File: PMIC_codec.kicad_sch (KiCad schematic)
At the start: 18 parts, among them U3 RK809-2

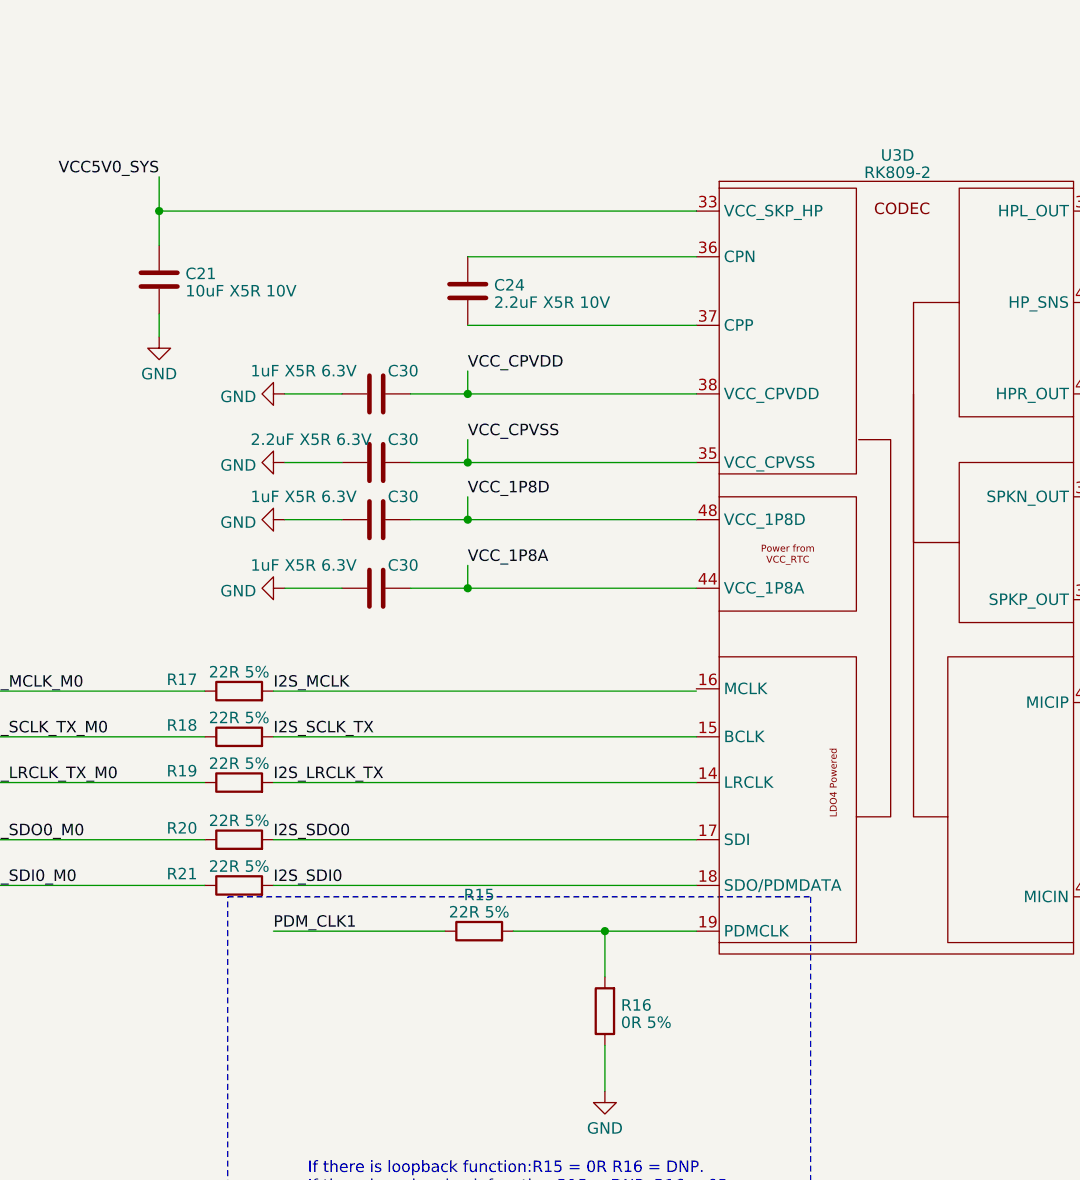
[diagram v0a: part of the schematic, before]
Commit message: updated footprints
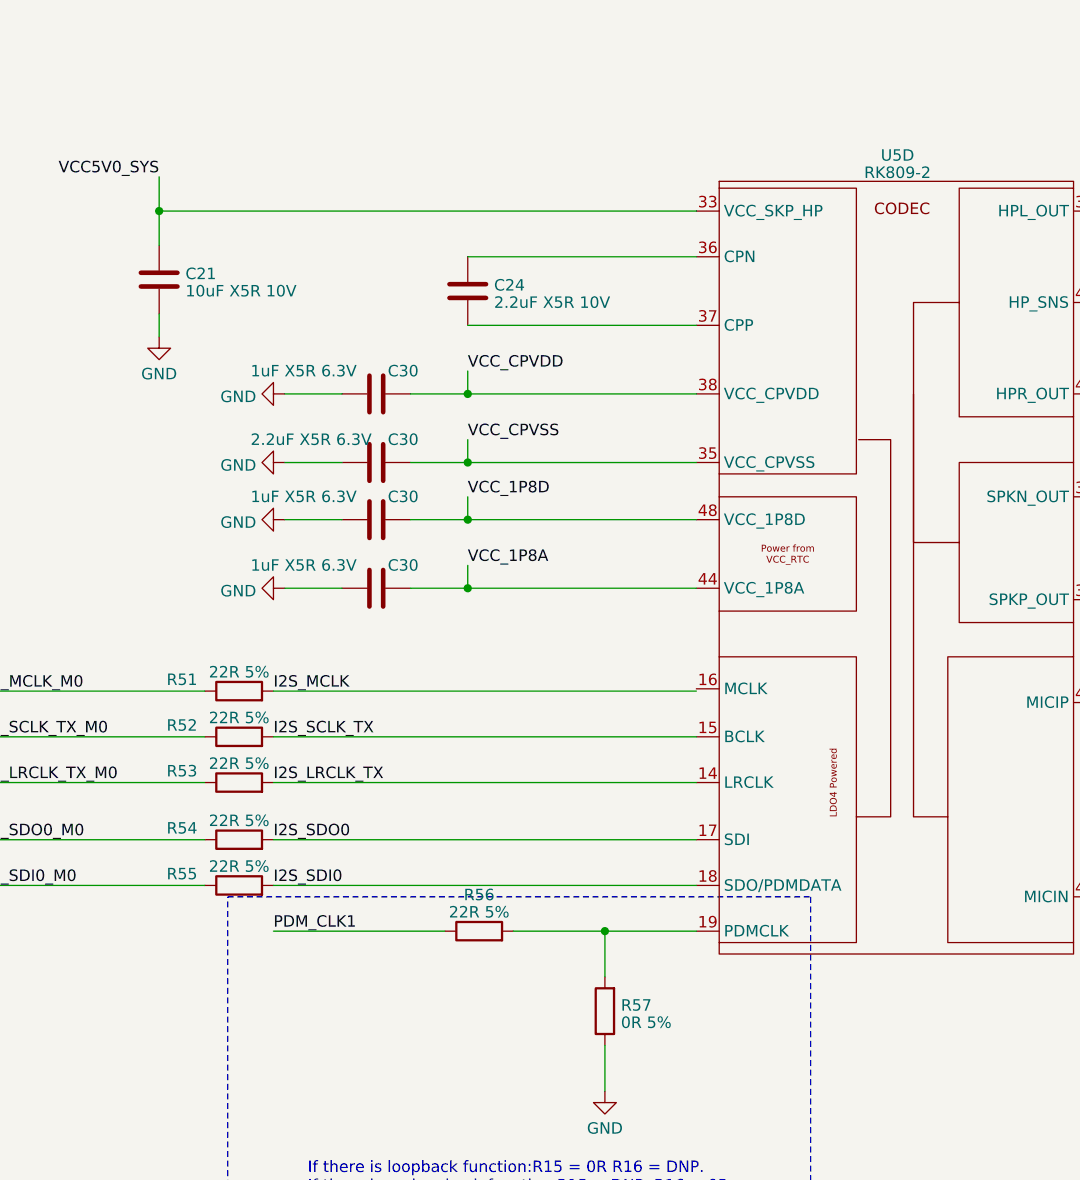
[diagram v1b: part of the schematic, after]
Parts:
- renumbered R17 to R51, R18 to R52, R19 to R53, R20 to R54, R21 to R55, R15 to R56, R16 to R57, U3 to U5
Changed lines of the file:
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@@
         )
         (path "/e3b58043-16a3-43c8-9fad-9c9784eebfa4/cc9fb3ac-19c3-47a8-ba7d-678b4d514ff0/46e9a7bf-8506-4399-90d8-57d007223126/932d3a83-3e3a-47a2-863a-dd551f528f64"
-          (reference "#PWR039") (unit 1)
+          (reference "#PWR0111") (unit 1)
         )
       )
@@
   (symbol (lib_id "CPU_Rockchip:RK809") (at 176.53 67.31 0) (unit 4)
     (in_bom yes) (on_board yes) (dnp no) (fields_autoplaced)
-    (property "Reference" "U3" (at 177.292 35.7251 0)
+    (property "Reference" "U5" (at 177.292 35.7251 0)
       (effects (font (size 1.27 1.27)))
     )
@@
       (project "leaf"
         (path "/e3b58043-16a3-43c8-9fad-9c9784eebfa4/cc9fb3ac-19c3-47a8-ba7d-678b4d514ff0/46e9a7bf-8506-4399-90d8-57d007223126/932d3a83-3e3a-47a2-863a-dd551f528f64"
-          (reference "U3") (unit 4)
+          (reference "U5") (unit 4)
         )
       )
@@
         )
         (path "/e3b58043-16a3-43c8-9fad-9c9784eebfa4/cc9fb3ac-19c3-47a8-ba7d-678b4d514ff0/46e9a7bf-8506-4399-90d8-57d007223126/932d3a83-3e3a-47a2-863a-dd551f528f64"
-          (reference "#PWR038") (unit 1)
+          (reference "#PWR0109") (unit 1)
         )
       )
@@
         )
         (path "/e3b58043-16a3-43c8-9fad-9c9784eebfa4/cc9fb3ac-19c3-47a8-ba7d-678b4d514ff0/46e9a7bf-8506-4399-90d8-57d007223126/932d3a83-3e3a-47a2-863a-dd551f528f64"
-          (reference "#PWR051") (unit 1)
+          (reference "#PWR0107") (unit 1)
         )
       )
@@
         )
         (path "/e3b58043-16a3-43c8-9fad-9c9784eebfa4/cc9fb3ac-19c3-47a8-ba7d-678b4d514ff0/46e9a7bf-8506-4399-90d8-57d007223126/932d3a83-3e3a-47a2-863a-dd551f528f64"
-          (reference "C46") (unit 1)
+          (reference "C89") (unit 1)
         )
       )
@@
         )
         (path "/e3b58043-16a3-43c8-9fad-9c9784eebfa4/cc9fb3ac-19c3-47a8-ba7d-678b4d514ff0/46e9a7bf-8506-4399-90d8-57d007223126/932d3a83-3e3a-47a2-863a-dd551f528f64"
-          (reference "C48") (unit 1)
+          (reference "C87") (unit 1)
         )
       )
@@
   (symbol (lib_id "Device:R") (at 104.14 111.76 90) (unit 1)
     (in_bom yes) (on_board yes) (dnp no)
-    (property "Reference" "R20" (at 97.79 110.49 90)
+    (property "Reference" "R54" (at 97.79 110.49 90)
       (effects (font (size 1.27 1.27)))
     )
@@
       (project "leaf"
         (path "/e3b58043-16a3-43c8-9fad-9c9784eebfa4/cc9fb3ac-19c3-47a8-ba7d-678b4d514ff0/46e9a7bf-8506-4399-90d8-57d007223126/932d3a83-3e3a-47a2-863a-dd551f528f64"
-          (reference "R20") (unit 1)
+          (reference "R54") (unit 1)
         )
       )
@@
   (symbol (lib_id "Device:R") (at 130.81 121.92 90) (unit 1)
     (in_bom yes) (on_board yes) (dnp no) (fields_autoplaced)
-    (property "Reference" "R15" (at 130.81 117.8941 90)
+    (property "Reference" "R56" (at 130.81 117.8941 90)
       (effects (font (size 1.27 1.27)))
     )
@@
       (project "leaf"
         (path "/e3b58043-16a3-43c8-9fad-9c9784eebfa4/cc9fb3ac-19c3-47a8-ba7d-678b4d514ff0/46e9a7bf-8506-4399-90d8-57d007223126/932d3a83-3e3a-47a2-863a-dd551f528f64"
-          (reference "R15") (unit 1)
+          (reference "R56") (unit 1)
         )
       )
@@
         )
         (path "/e3b58043-16a3-43c8-9fad-9c9784eebfa4/cc9fb3ac-19c3-47a8-ba7d-678b4d514ff0/46e9a7bf-8506-4399-90d8-57d007223126/932d3a83-3e3a-47a2-863a-dd551f528f64"
-          (reference "C43") (unit 1)
+          (reference "C83") (unit 1)
         )
       )
@@
         )
         (path "/e3b58043-16a3-43c8-9fad-9c9784eebfa4/cc9fb3ac-19c3-47a8-ba7d-678b4d514ff0/46e9a7bf-8506-4399-90d8-57d007223126/932d3a83-3e3a-47a2-863a-dd551f528f64"
-          (reference "#PWR052") (unit 1)
+          (reference "#PWR0106") (unit 1)
         )
       )
@@
         )
         (path "/e3b58043-16a3-43c8-9fad-9c9784eebfa4/cc9fb3ac-19c3-47a8-ba7d-678b4d514ff0/46e9a7bf-8506-4399-90d8-57d007223126/932d3a83-3e3a-47a2-863a-dd551f528f64"
-          (reference "#PWR053") (unit 1)
+          (reference "#PWR0105") (unit 1)
         )
       )
@@
         )
         (path "/e3b58043-16a3-43c8-9fad-9c9784eebfa4/cc9fb3ac-19c3-47a8-ba7d-678b4d514ff0/46e9a7bf-8506-4399-90d8-57d007223126/932d3a83-3e3a-47a2-863a-dd551f528f64"
-          (reference "#PWR050") (unit 1)
+          (reference "#PWR0104") (unit 1)
         )
       )
@@
         )
         (path "/e3b58043-16a3-43c8-9fad-9c9784eebfa4/cc9fb3ac-19c3-47a8-ba7d-678b4d514ff0/46e9a7bf-8506-4399-90d8-57d007223126/932d3a83-3e3a-47a2-863a-dd551f528f64"
-          (reference "C45") (unit 1)
+          (reference "C88") (unit 1)
         )
       )
@@
         )
         (path "/e3b58043-16a3-43c8-9fad-9c9784eebfa4/cc9fb3ac-19c3-47a8-ba7d-678b4d514ff0/46e9a7bf-8506-4399-90d8-57d007223126/932d3a83-3e3a-47a2-863a-dd551f528f64"
-          (reference "C39") (unit 1)
+          (reference "C80") (unit 1)
         )
       )
@@
         )
         (path "/e3b58043-16a3-43c8-9fad-9c9784eebfa4/cc9fb3ac-19c3-47a8-ba7d-678b4d514ff0/46e9a7bf-8506-4399-90d8-57d007223126/932d3a83-3e3a-47a2-863a-dd551f528f64"
-          (reference "C40") (unit 1)
+          (reference "C85") (unit 1)
         )
       )
@@
   (symbol (lib_id "Device:R") (at 104.14 95.25 90) (unit 1)
     (in_bom yes) (on_board yes) (dnp no)
-    (property "Reference" "R17" (at 97.79 93.98 90)
+    (property "Reference" "R51" (at 97.79 93.98 90)
       (effects (font (size 1.27 1.27)))
     )
@@
       (project "leaf"
         (path "/e3b58043-16a3-43c8-9fad-9c9784eebfa4/cc9fb3ac-19c3-47a8-ba7d-678b4d514ff0/46e9a7bf-8506-4399-90d8-57d007223126/932d3a83-3e3a-47a2-863a-dd551f528f64"
-          (reference "R17") (unit 1)
+          (reference "R51") (unit 1)
         )
       )
@@
         )
         (path "/e3b58043-16a3-43c8-9fad-9c9784eebfa4/cc9fb3ac-19c3-47a8-ba7d-678b4d514ff0/46e9a7bf-8506-4399-90d8-57d007223126/932d3a83-3e3a-47a2-863a-dd551f528f64"
-          (reference "#PWR054") (unit 1)
+          (reference "#PWR0108") (unit 1)
         )
       )
@@
         )
         (path "/e3b58043-16a3-43c8-9fad-9c9784eebfa4/cc9fb3ac-19c3-47a8-ba7d-678b4d514ff0/46e9a7bf-8506-4399-90d8-57d007223126/932d3a83-3e3a-47a2-863a-dd551f528f64"
-          (reference "C41") (unit 1)
+          (reference "C81") (unit 1)
         )
       )
@@
         )
         (path "/e3b58043-16a3-43c8-9fad-9c9784eebfa4/cc9fb3ac-19c3-47a8-ba7d-678b4d514ff0/46e9a7bf-8506-4399-90d8-57d007223126/932d3a83-3e3a-47a2-863a-dd551f528f64"
-          (reference "C47") (unit 1)
+          (reference "C86") (unit 1)
         )
       )
@@
   (symbol (lib_id "Device:R") (at 104.14 100.33 90) (unit 1)
     (in_bom yes) (on_board yes) (dnp no)
-    (property "Reference" "R18" (at 97.79 99.06 90)
+    (property "Reference" "R52" (at 97.79 99.06 90)
       (effects (font (size 1.27 1.27)))
     )
@@
       (project "leaf"
         (path "/e3b58043-16a3-43c8-9fad-9c9784eebfa4/cc9fb3ac-19c3-47a8-ba7d-678b4d514ff0/46e9a7bf-8506-4399-90d8-57d007223126/932d3a83-3e3a-47a2-863a-dd551f528f64"
-          (reference "R18") (unit 1)
+          (reference "R52") (unit 1)
         )
       )
@@
         )
         (path "/e3b58043-16a3-43c8-9fad-9c9784eebfa4/cc9fb3ac-19c3-47a8-ba7d-678b4d514ff0/46e9a7bf-8506-4399-90d8-57d007223126/932d3a83-3e3a-47a2-863a-dd551f528f64"
-          (reference "C42") (unit 1)
+          (reference "C82") (unit 1)
         )
       )
@@
   (symbol (lib_id "Device:R") (at 144.78 130.81 180) (unit 1)
     (in_bom yes) (on_board yes) (dnp no) (fields_autoplaced)
-    (property "Reference" "R16" (at 146.558 130.1663 0)
+    (property "Reference" "R57" (at 146.558 130.1663 0)
       (effects (font (size 1.27 1.27)) (justify right))
     )
@@
       (project "leaf"
         (path "/e3b58043-16a3-43c8-9fad-9c9784eebfa4/cc9fb3ac-19c3-47a8-ba7d-678b4d514ff0/46e9a7bf-8506-4399-90d8-57d007223126/932d3a83-3e3a-47a2-863a-dd551f528f64"
-          (reference "R16") (unit 1)
+          (reference "R57") (unit 1)
         )
       )
@@
         )
         (path "/e3b58043-16a3-43c8-9fad-9c9784eebfa4/cc9fb3ac-19c3-47a8-ba7d-678b4d514ff0/46e9a7bf-8506-4399-90d8-57d007223126/932d3a83-3e3a-47a2-863a-dd551f528f64"
-          (reference "#PWR049") (unit 1)
+          (reference "#PWR0110") (unit 1)
         )
       )
@@
   (symbol (lib_id "Device:R") (at 104.14 105.41 90) (unit 1)
     (in_bom yes) (on_board yes) (dnp no)
-    (property "Reference" "R19" (at 97.79 104.14 90)
+    (property "Reference" "R53" (at 97.79 104.14 90)
       (effects (font (size 1.27 1.27)))
     )
@@
       (project "leaf"
         (path "/e3b58043-16a3-43c8-9fad-9c9784eebfa4/cc9fb3ac-19c3-47a8-ba7d-678b4d514ff0/46e9a7bf-8506-4399-90d8-57d007223126/932d3a83-3e3a-47a2-863a-dd551f528f64"
-          (reference "R19") (unit 1)
+          (reference "R53") (unit 1)
         )
       )
@@
         )
         (path "/e3b58043-16a3-43c8-9fad-9c9784eebfa4/cc9fb3ac-19c3-47a8-ba7d-678b4d514ff0/46e9a7bf-8506-4399-90d8-57d007223126/932d3a83-3e3a-47a2-863a-dd551f528f64"
-          (reference "C44") (unit 1)
+          (reference "C84") (unit 1)
         )
       )
@@
   (symbol (lib_id "Device:R") (at 104.14 116.84 90) (unit 1)
     (in_bom yes) (on_board yes) (dnp no)
-    (property "Reference" "R21" (at 97.79 115.57 90)
+    (property "Reference" "R55" (at 97.79 115.57 90)
       (effects (font (size 1.27 1.27)))
     )
@@
       (project "leaf"
         (path "/e3b58043-16a3-43c8-9fad-9c9784eebfa4/cc9fb3ac-19c3-47a8-ba7d-678b4d514ff0/46e9a7bf-8506-4399-90d8-57d007223126/932d3a83-3e3a-47a2-863a-dd551f528f64"
-          (reference "R21") (unit 1)
-        )
-      )
+          (reference "R55") (unit 1)
+        )
+      )

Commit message: updated Capacitors
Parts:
- C21: LCSC (none) -> C469532; Model (none) -> GRM188B31A106KE69D; Vendor (none) -> muRata(村田)
- C30: footprint Capacitor_SMD:C_0402_1005Metric -> Capacitor_SMD:C_0201_0603Metric; LCSC (none) -> C76929; Model (none) -> GRM033R60J105KEA2D; Vendor (none) -> muRata(村田)
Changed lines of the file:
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@@
       (effects (font (size 1.27 1.27)) (justify left))
     )
-    (property "Footprint" "Capacitor_SMD:C_0402_1005Metric" (at 115.57 75.2348 0)
+    (property "Footprint" "Capacitor_SMD:C_0201_0603Metric" (at 115.57 75.2348 0)
       (effects (font (size 1.27 1.27)) hide)
     )
     (property "Datasheet" "~" (at 119.38 76.2 0)
+      (effects (font (size 1.27 1.27)) hide)
+    )
+    (property "Description" "容值: 1uF 精度: ±10% 额定电压: 6.3V 材质(温度系数): X5R 材质:X5R" (at 119.38 76.2 0)
+      (effects (font (size 1.27 1.27)) hide)
+    )
+    (property "LCSC" "C76929" (at 119.38 76.2 0)
+      (effects (font (size 1.27 1.27)) hide)
+    )
+    (property "Model" "GRM033R60J105KEA2D" (at 119.38 76.2 0)
+      (effects (font (size 1.27 1.27)) hide)
+    )
+    (property "Vendor" "muRata(村田)" (at 119.38 76.2 0)
       (effects (font (size 1.27 1.27)) hide)
     )
@@
       (effects (font (size 1.27 1.27)) hide)
     )
+    (property "Description" "容值: 10uF 精度: ±10% 额定电压: 10V 材质(温度系数): B B(JIS)" (at 95.25 49.53 0)
+      (effects (font (size 1.27 1.27)) hide)
+    )
+    (property "LCSC" "C469532" (at 95.25 49.53 0)
+      (effects (font (size 1.27 1.27)) hide)
+    )
+    (property "Model" "GRM188B31A106KE69D" (at 95.25 49.53 0)
+      (effects (font (size 1.27 1.27)) hide)
+    )
+    (property "Vendor" "muRata(村田)" (at 95.25 49.53 0)
+      (effects (font (size 1.27 1.27)) hide)
+    )
     (pin "1")
     (pin "2")
@@
       (effects (font (size 1.27 1.27)) (justify left))
     )
-    (property "Footprint" "Capacitor_SMD:C_0402_1005Metric" (at 115.57 61.2648 0)
+    (property "Footprint" "Capacitor_SMD:C_0201_0603Metric" (at 115.57 61.2648 0)
       (effects (font (size 1.27 1.27)) hide)
     )
     (property "Datasheet" "~" (at 119.38 62.23 0)
+      (effects (font (size 1.27 1.27)) hide)
+    )
+    (property "Description" "容值: 1uF 精度: ±10% 额定电压: 6.3V 材质(温度系数): X5R 材质:X5R" (at 119.38 62.23 0)
+      (effects (font (size 1.27 1.27)) hide)
+    )
+    (property "LCSC" "C76929" (at 119.38 62.23 0)
+      (effects (font (size 1.27 1.27)) hide)
+    )
+    (property "Model" "GRM033R60J105KEA2D" (at 119.38 62.23 0)
+      (effects (font (size 1.27 1.27)) hide)
+    )
+    (property "Vendor" "muRata(村田)" (at 119.38 62.23 0)
       (effects (font (size 1.27 1.27)) hide)
     )
@@
       (effects (font (size 1.27 1.27)) (justify left))
     )
-    (property "Footprint" "Capacitor_SMD:C_0402_1005Metric" (at 115.57 82.8548 0)
+    (property "Footprint" "Capacitor_SMD:C_0201_0603Metric" (at 115.57 82.8548 0)
       (effects (font (size 1.27 1.27)) hide)
     )
@@
       (effects (font (size 1.27 1.27)) hide)
     )
+    (property "Description" "容值: 1uF 精度: ±10% 额定电压: 6.3V 材质(温度系数): X5R 材质:X5R" (at 119.38 83.82 0)
+      (effects (font (size 1.27 1.27)) hide)
+    )
+    (property "LCSC" "C76929" (at 119.38 83.82 0)
+      (effects (font (size 1.27 1.27)) hide)
+    )
+    (property "Model" "GRM033R60J105KEA2D" (at 119.38 83.82 0)
+      (effects (font (size 1.27 1.27)) hide)
+    )
+    (property "Vendor" "muRata(村田)" (at 119.38 83.82 0)
+      (effects (font (size 1.27 1.27)) hide)
+    )
